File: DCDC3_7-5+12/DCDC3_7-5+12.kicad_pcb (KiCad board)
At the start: 2 copper layers, 63.5 x 75.8 mm, 34 parts, among them J1 FAN, Q1 CSD16323Q3, T1 + 3.7V -, T2 + 12V -, T3 + 5V -, U1 LM3488, U2 XL6009

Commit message: Final version of aux 5v and 12v power supply.
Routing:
- net Net-(D2-Pad2): track 32.8 -> 54.7 mm, vias 5 -> 11
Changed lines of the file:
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@@
     (links 62)
     (no_connects 0)
-    (area 101.524999 63.424999 165.175001 139.375001)
+    (area 93.769977 54.45 183.11 142.240001)
     (thickness 1.6)
     (drawings 12)
-    (tracks 204)
+    (tracks 233)
     (zones 0)
     (modules 34)
@@
   )
   (setup
-    (last_trace_width 0.25)
+    (last_trace_width 0.5)
     (user_trace_width 0.5)
     (user_trace_width 1)
@@
   (via (at 104.648 109.474) (size 0.6) (drill 0.4) (layers F.Cu B.Cu) (net 2))
   (via (at 110.744 109.728) (size 0.6) (drill 0.4) (layers F.Cu B.Cu) (net 2))
-  (segment (start 143.096 104.902) (end 139.7 104.902) (width 0.5) (layer F.Cu) (net 4))
-  (via (at 139.7 104.902) (size 1.2) (drill 0.8) (layers F.Cu B.Cu) (net 4))
+  (segment (start 141.478 102.616) (end 143.764 102.616) (width 0.5) (layer B.Cu) (net 4))
+  (via (at 143.764 102.616) (size 1.2) (drill 0.8) (layers F.Cu B.Cu) (net 4))
+  (segment (start 140.878001 103.215999) (end 141.478 102.616) (width 0.5) (layer B.Cu) (net 4))
+  (segment (start 139.7 104.14) (end 139.954 104.14) (width 0.5) (layer B.Cu) (net 4))
+  (segment (start 139.954 104.14) (end 140.878001 103.215999) (width 0.5) (layer B.Cu) (net 4))
+  (via (at 141.478 102.616) (size 1.2) (drill 0.8) (layers F.Cu B.Cu) (net 4))
+  (segment (start 141.732 107.442) (end 143.764 107.442) (width 0.5) (layer F.Cu) (net 4))
+  (via (at 143.764 107.442) (size 1.2) (drill 0.8) (layers F.Cu B.Cu) (net 4))
+  (segment (start 139.954002 104.902) (end 139.7 105.156002) (width 0.5) (layer F.Cu) (net 4))
+  (segment (start 139.7 106.00453) (end 139.7 105.156002) (width 0.25) (layer F.Cu) (net 4))
+  (segment (start 143.096 104.902) (end 139.954002 104.902) (width 0.5) (layer F.Cu) (net 4))
+  (segment (start 139.7 106.172) (end 139.7 106.00453) (width 0.25) (layer F.Cu) (net 4))
+  (segment (start 139.446 106.426) (end 139.7 106.172) (width 0.25) (layer F.Cu) (net 4))
+  (segment (start 139.7 104.648) (end 139.7 105.156002) (width 0.5) (layer B.Cu) (net 4))
+  (via (at 139.7 105.156002) (size 1.2) (drill 0.8) (layers F.Cu B.Cu) (net 4))
+  (segment (start 139.7 104.14) (end 139.7 104.648) (width 0.5) (layer B.Cu) (net 4))
+  (segment (start 140.300001 106.842001) (end 139.700002 107.442) (width 0.5) (layer F.Cu) (net 4))
+  (segment (start 140.462002 106.68) (end 140.300001 106.842001) (width 0.5) (layer F.Cu) (net 4))
+  (segment (start 140.97 106.68) (end 140.462002 106.68) (width 0.5) (layer F.Cu) (net 4))
+  (segment (start 139.7 104.14) (end 139.700002 104.140002) (width 0.5) (layer B.Cu) (net 4))
+  (segment (start 139.700002 104.140002) (end 139.700002 106.593472) (width 0.5) (layer B.Cu) (net 4))
+  (segment (start 139.700002 106.593472) (end 139.700002 107.442) (width 0.5) (layer B.Cu) (net 4))
+  (segment (start 139.7 107.441998) (end 139.700002 107.442) (width 0.5) (layer F.Cu) (net 4))
+  (segment (start 141.732 107.442) (end 140.97 106.68) (width 0.5) (layer F.Cu) (net 4))
+  (segment (start 139.7 106.68) (end 139.7 107.441998) (width 0.5) (layer F.Cu) (net 4))
+  (segment (start 141.224 106.426) (end 140.97 106.68) (width 0.5) (layer F.Cu) (net 4))
+  (segment (start 139.7 102.616) (end 139.7 106.68) (width 0.5) (layer F.Cu) (net 4))
+  (via (at 139.700002 107.442) (size 1.2) (drill 0.8) (layers F.Cu B.Cu) (net 4))
+  (via (at 141.732 107.442) (size 1.2) (drill 0.8) (layers F.Cu B.Cu) (net 4))
+  (segment (start 139.7 102.616) (end 139.7 104.14) (width 0.5) (layer B.Cu) (net 4))
+  (via (at 139.7 102.616) (size 1.2) (drill 0.8) (layers F.Cu B.Cu) (net 4))
   (segment (start 148.59 82.14) (end 150.94 82.14) (width 1) (layer F.Cu) (net 4))
   (segment (start 155.055 90.98) (end 155.055 94.605) (width 1) (layer F.Cu) (net 4))
@@
     (polygon
       (pts
-        (xy 163.83 88.9) (xy 163.83 107.95) (xy 138.43 107.95) (xy 138.43 88.9)
+        (xy 165.608 88.9) (xy 165.608 108.712) (xy 138.43 108.712) (xy 138.43 101.854) (xy 138.43 88.9)
       )
     )
@@
     (polygon
       (pts
-        (xy 125.73 65.532) (xy 163.576 65.532) (xy 163.83 76.962) (xy 146.558 76.962) (xy 146.558 102.108)
-        (xy 137.668 102.108) (xy 137.668 134.62) (xy 125.73 134.62)
+        (xy 125.984 61.722) (xy 166.624 61.722) (xy 166.624 76.962) (xy 146.558 76.962) (xy 146.558 101.346)
+        (xy 137.668 101.346) (xy 137.414 141.986) (xy 125.73 141.732)
       )
     )
@@
     (polygon
       (pts
-        (xy 163.83 103.378) (xy 163.83 135.89) (xy 138.43 135.89) (xy 138.43 103.378)
+        (xy 166.116 103.632) (xy 166.116 142.24) (xy 138.43 142.24) (xy 138.43 109.982) (xy 146.558 109.982)
+        (xy 146.558 102.362) (xy 151.13 102.362) (xy 151.13 103.632)
       )
     )
@@
     (polygon
       (pts
-        (xy 109.22 88.392) (xy 102.616 88.392) (xy 102.616 138.176) (xy 111.506 138.176) (xy 111.506 129.032)
+        (xy 109.22 88.392) (xy 101.346 88.392) (xy 101.6 140.208) (xy 111.506 140.208) (xy 111.506 129.032)
         (xy 105.918 129.032) (xy 105.918 93.98) (xy 109.22 93.98)
       )
@@
     (polygon
       (pts
-        (xy 125.222 65.024) (xy 102.87 65.024) (xy 102.87 87.63) (xy 110.236 87.63) (xy 110.236 94.742)
+        (xy 125.222 61.214) (xy 101.6 61.214) (xy 101.6 87.63) (xy 110.236 87.63) (xy 110.236 94.742)
         (xy 115.57 94.742) (xy 115.57 100.584) (xy 120.142 100.584) (xy 120.142 94.742) (xy 125.222 94.742)
       )
@@
     (polygon
       (pts
-        (xy 125.222 95.25) (xy 125.222 138.684) (xy 112.014 138.684) (xy 112.268 138.684) (xy 112.268 128.524)
+        (xy 125.222 95.25) (xy 124.714 141.986) (xy 112.268 141.986) (xy 112.268 138.684) (xy 112.268 128.524)
         (xy 106.426 128.524) (xy 106.426 95.25) (xy 110.998 95.25) (xy 110.998 100.076) (xy 111.506 100.076)
         (xy 111.506 102.362) (xy 114.554 102.362) (xy 114.554 101.092) (xy 120.65 101.092) (xy 120.65 95.25)
@@
     (polygon
       (pts
-        (xy 147.32 77.724) (xy 164.338 77.724) (xy 164.338 102.616) (xy 148.082 102.616) (xy 148.082 91.44)
-        (xy 147.32 91.44)
+        (xy 147.32 77.724) (xy 166.37 77.724) (xy 166.37 103.124) (xy 151.892 103.124) (xy 151.892 101.854)
+        (xy 148.082 101.854) (xy 148.082 91.44) (xy 147.32 91.44)
       )
     )
+  )
+  (zone (net 4) (net_name "Net-(D2-Pad2)") (layer F.Cu) (hatch edge 0.508)
+    (connect_pads yes (clearance 0.508))
+    (min_thickness 0.254)
+    (fill yes (arc_segments 16) (thermal_gap 0.508) (thermal_bridge_width 0.508))
+    (polygon
+      (pts
+        (xy 138.43 101.854) (xy 145.796 101.854) (xy 145.796 109.474) (xy 138.43 109.474)
+      )
+    )

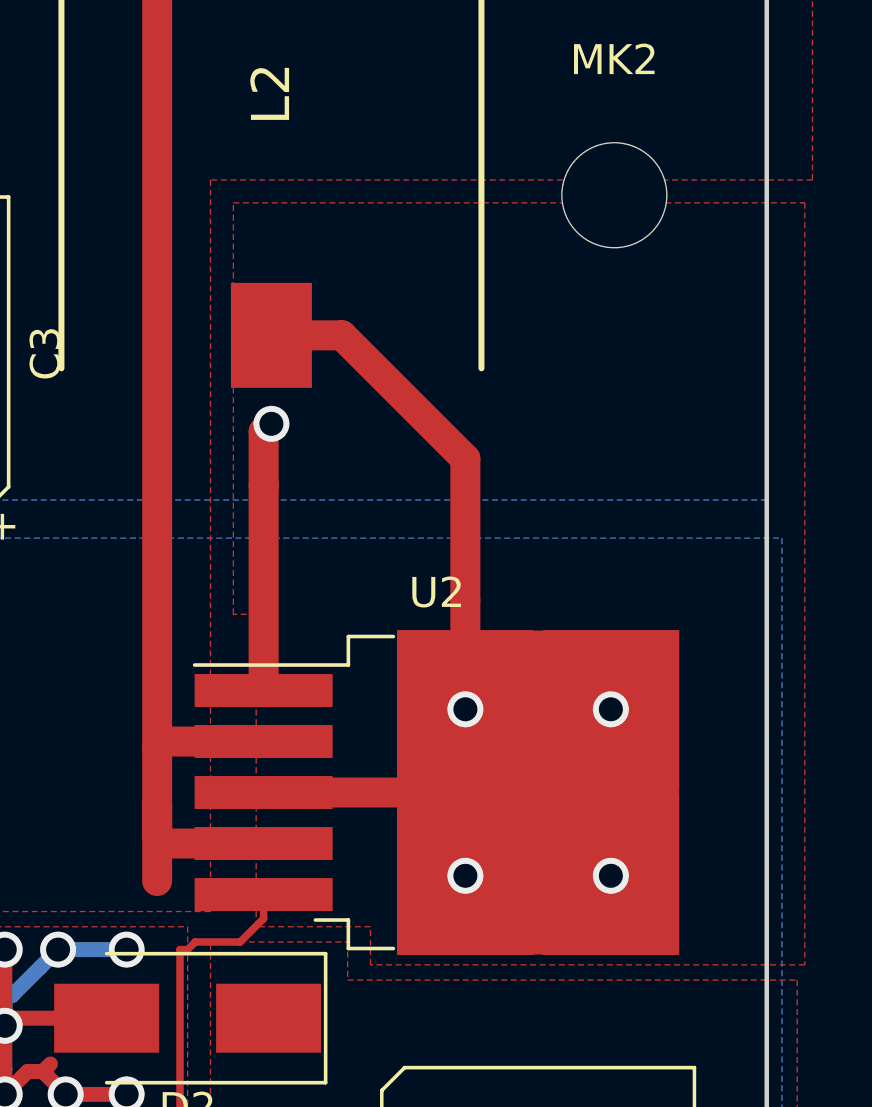
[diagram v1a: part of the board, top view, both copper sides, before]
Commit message: Final version of aux 5v and 12v power supply.
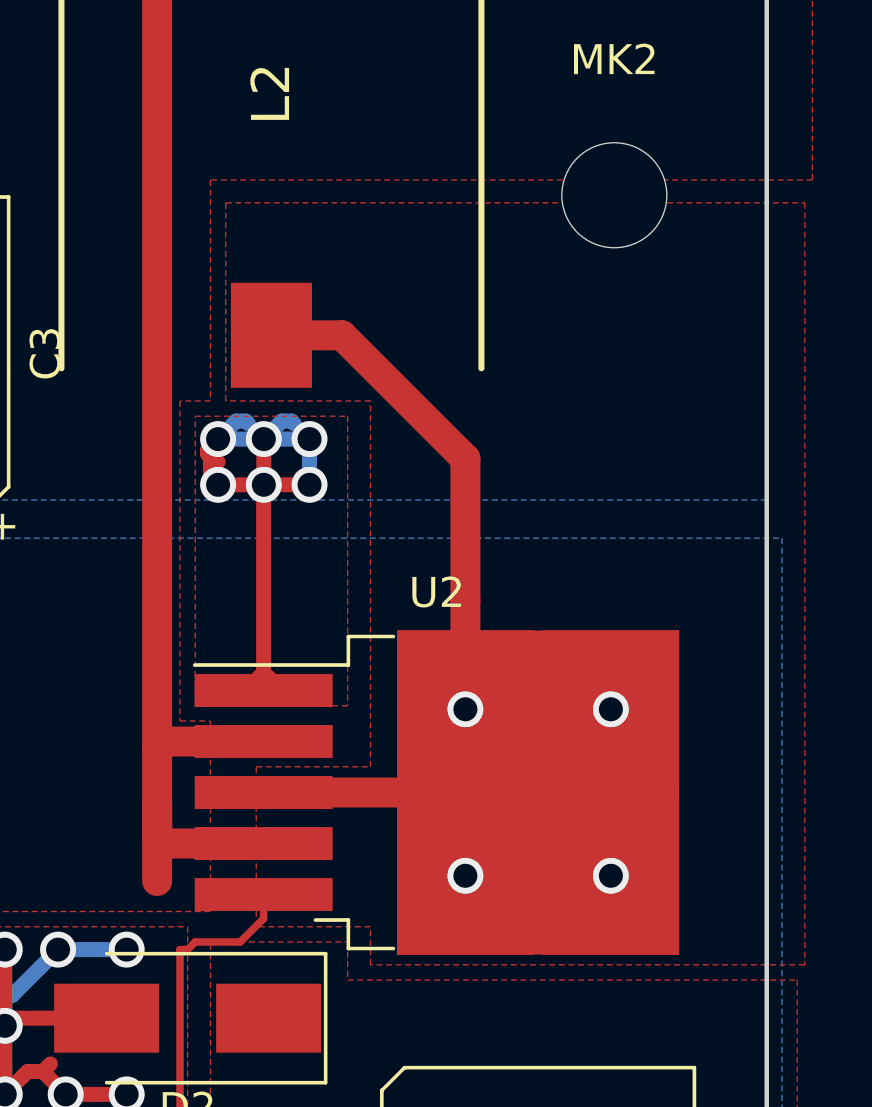
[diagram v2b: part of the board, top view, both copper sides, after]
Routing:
- net GND: track 74.5 -> 87.0 mm, vias 43 -> 48
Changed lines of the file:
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@@
     (links 62)
     (no_connects 0)
-    (area 93.769977 54.45 183.11 142.240001)
+    (area 101.524999 63.424999 165.175001 139.375001)
     (thickness 1.6)
     (drawings 12)
-    (tracks 233)
+    (tracks 260)
     (zones 0)
     (modules 34)
@@
   (segment (start 143.764 114.474) (end 143.764 112.268) (width 0.25) (layer F.Cu) (net 5))
   (segment (start 143.764 112.268) (end 144.272 111.76) (width 0.25) (layer F.Cu) (net 5))
+  (segment (start 147.736003 84.998003) (end 147.411999 84.998003) (width 0.5) (layer B.Cu) (net 6))
+  (segment (start 147.828 85.09) (end 147.736003 84.998003) (width 0.5) (layer B.Cu) (net 6))
+  (segment (start 146.466001 85.944001) (end 146.812 85.598002) (width 0.5) (layer F.Cu) (net 6))
+  (segment (start 146.466001 86.100529) (end 146.466001 85.944001) (width 0.5) (layer F.Cu) (net 6))
+  (segment (start 146.558 86.192528) (end 146.466001 86.100529) (width 0.5) (layer F.Cu) (net 6))
+  (segment (start 146.812002 85.598) (end 146.812 85.598002) (width 0.5) (layer B.Cu) (net 6))
+  (segment (start 148.336 85.598) (end 146.812002 85.598) (width 0.5) (layer B.Cu) (net 6))
+  (segment (start 147.411999 84.998003) (end 146.812 85.598002) (width 0.5) (layer B.Cu) (net 6))
+  (via (at 146.812 85.598002) (size 1.2) (drill 0.8) (layers F.Cu B.Cu) (net 6))
+  (segment (start 146.812 87.121998) (end 146.558 86.867998) (width 0.5) (layer F.Cu) (net 6))
+  (segment (start 146.558 86.867998) (end 146.558 86.192528) (width 0.5) (layer F.Cu) (net 6))
+  (segment (start 146.812 86.36) (end 146.725472 86.36) (width 0.5) (layer F.Cu) (net 6))
+  (segment (start 146.725472 86.36) (end 146.558 86.192528) (width 0.5) (layer F.Cu) (net 6))
+  (segment (start 149.352 85.09) (end 149.260001 84.998001) (width 0.5) (layer B.Cu) (net 6))
+  (segment (start 149.86 85.598) (end 148.336 85.598) (width 0.5) (layer B.Cu) (net 6))
+  (segment (start 148.935999 84.998001) (end 148.336 85.598) (width 0.5) (layer B.Cu) (net 6))
+  (via (at 148.336 85.598) (size 1.2) (drill 0.8) (layers F.Cu B.Cu) (net 6))
+  (segment (start 149.260001 84.998001) (end 148.935999 84.998001) (width 0.5) (layer B.Cu) (net 6))
+  (segment (start 148.336 87.121998) (end 148.336 85.598) (width 0.5) (layer F.Cu) (net 6))
+  (segment (start 149.86 87.121992) (end 149.86 85.598) (width 0.5) (layer B.Cu) (net 6))
+  (segment (start 149.86 86.36) (end 149.86 85.598) (width 0.5) (layer B.Cu) (net 6))
+  (via (at 149.86 85.598) (size 1.2) (drill 0.8) (layers F.Cu B.Cu) (net 6))
+  (segment (start 148.336 87.121998) (end 146.812 87.121998) (width 0.5) (layer F.Cu) (net 6))
+  (segment (start 146.812 87.121998) (end 146.811998 87.122) (width 0.5) (layer F.Cu) (net 6))
+  (via (at 146.811998 87.122) (size 1.2) (drill 0.8) (layers F.Cu B.Cu) (net 6))
+  (segment (start 148.336006 87.121992) (end 148.336 87.121998) (width 0.5) (layer F.Cu) (net 6))
+  (segment (start 149.86 87.121992) (end 148.336006 87.121992) (width 0.5) (layer F.Cu) (net 6))
+  (segment (start 148.33 87.127998) (end 148.336 87.121998) (width 0.5) (layer F.Cu) (net 6))
+  (segment (start 148.33 93.98) (end 148.33 87.127998) (width 0.5) (layer F.Cu) (net 6))
+  (via (at 148.336 87.121998) (size 1.2) (drill 0.8) (layers F.Cu B.Cu) (net 6))
+  (via (at 149.86 87.121992) (size 1.2) (drill 0.8) (layers F.Cu B.Cu) (net 6))
   (segment (start 123.952 101.092) (end 124.714 101.092) (width 0.25) (layer B.Cu) (net 6))
   (via (at 124.714 101.092) (size 0.6) (drill 0.4) (layers F.Cu B.Cu) (net 6))
@@
   (segment (start 161.48 111.76) (end 161.48 121.73) (width 1) (layer F.Cu) (net 6))
   (segment (start 161.48 121.73) (end 160.02 123.19) (width 1) (layer F.Cu) (net 6))
-  (segment (start 148.33 87.14) (end 148.33 85.35) (width 1) (layer F.Cu) (net 6))
-  (segment (start 148.33 85.35) (end 148.59 85.09) (width 1) (layer F.Cu) (net 6))
-  (via (at 148.59 85.09) (size 1.2) (drill 0.8) (layers F.Cu B.Cu) (net 6))
   (segment (start 132.37 72.39) (end 132.37 76.49) (width 1) (layer F.Cu) (net 6))
   (via (at 132.37 72.39) (size 1.2) (drill 0.8) (layers F.Cu B.Cu) (net 6))
   (segment (start 132.37 76.49) (end 134.62 78.74) (width 1) (layer F.Cu) (net 6))
-  (segment (start 148.33 93.98) (end 148.33 87.14) (width 1) (layer F.Cu) (net 6))
   (segment (start 148.59 93.98) (end 148.33 93.98) (width 1) (layer F.Cu) (net 6))
   (segment (start 148.33 93.98) (end 148.33 93.72) (width 1) (layer F.Cu) (net 6))
@@
     (polygon
       (pts
-        (xy 125.984 61.722) (xy 166.624 61.722) (xy 166.624 76.962) (xy 146.558 76.962) (xy 146.558 101.346)
-        (xy 137.668 101.346) (xy 137.414 141.986) (xy 125.73 141.732)
+        (xy 125.984 61.722) (xy 166.624 61.722) (xy 166.624 76.962) (xy 146.558 76.962) (xy 146.558 84.328)
+        (xy 145.542 84.328) (xy 145.542 94.996) (xy 146.558 94.996) (xy 146.558 101.346) (xy 137.668 101.346)
+        (xy 137.414 141.986) (xy 125.73 141.732)
       )
     )
@@
     (polygon
       (pts
-        (xy 147.32 77.724) (xy 166.37 77.724) (xy 166.37 103.124) (xy 151.892 103.124) (xy 151.892 101.854)
-        (xy 148.082 101.854) (xy 148.082 91.44) (xy 147.32 91.44)
+        (xy 147.066 77.724) (xy 166.37 77.724) (xy 166.37 103.124) (xy 151.892 103.124) (xy 151.892 101.854)
+        (xy 148.082 101.854) (xy 148.082 96.52) (xy 151.892 96.52) (xy 151.892 84.328) (xy 147.066 84.328)
       )
     )
@@
       )
     )
+  )
+  (zone (net 6) (net_name GND) (layer F.Cu) (hatch edge 0.508)
+    (connect_pads yes (clearance 0.508))
+    (min_thickness 0.254)
+    (fill yes (arc_segments 16) (thermal_gap 0.508) (thermal_bridge_width 0.508))
+    (polygon
+      (pts
+        (xy 151.13 84.836) (xy 151.13 94.488) (xy 146.05 94.488) (xy 146.05 84.836)
+      )
+    )
